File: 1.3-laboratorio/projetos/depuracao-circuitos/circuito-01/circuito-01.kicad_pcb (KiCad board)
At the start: 2 copper layers, 63.5 x 58.4 mm, 19 parts, among them J1 J1, J2 J2, J3 J3, J4 J4, P1 CONN_01X02, SW1 SW_DIP_x04, U1 74LS32, U2 7400, U3 74LS386

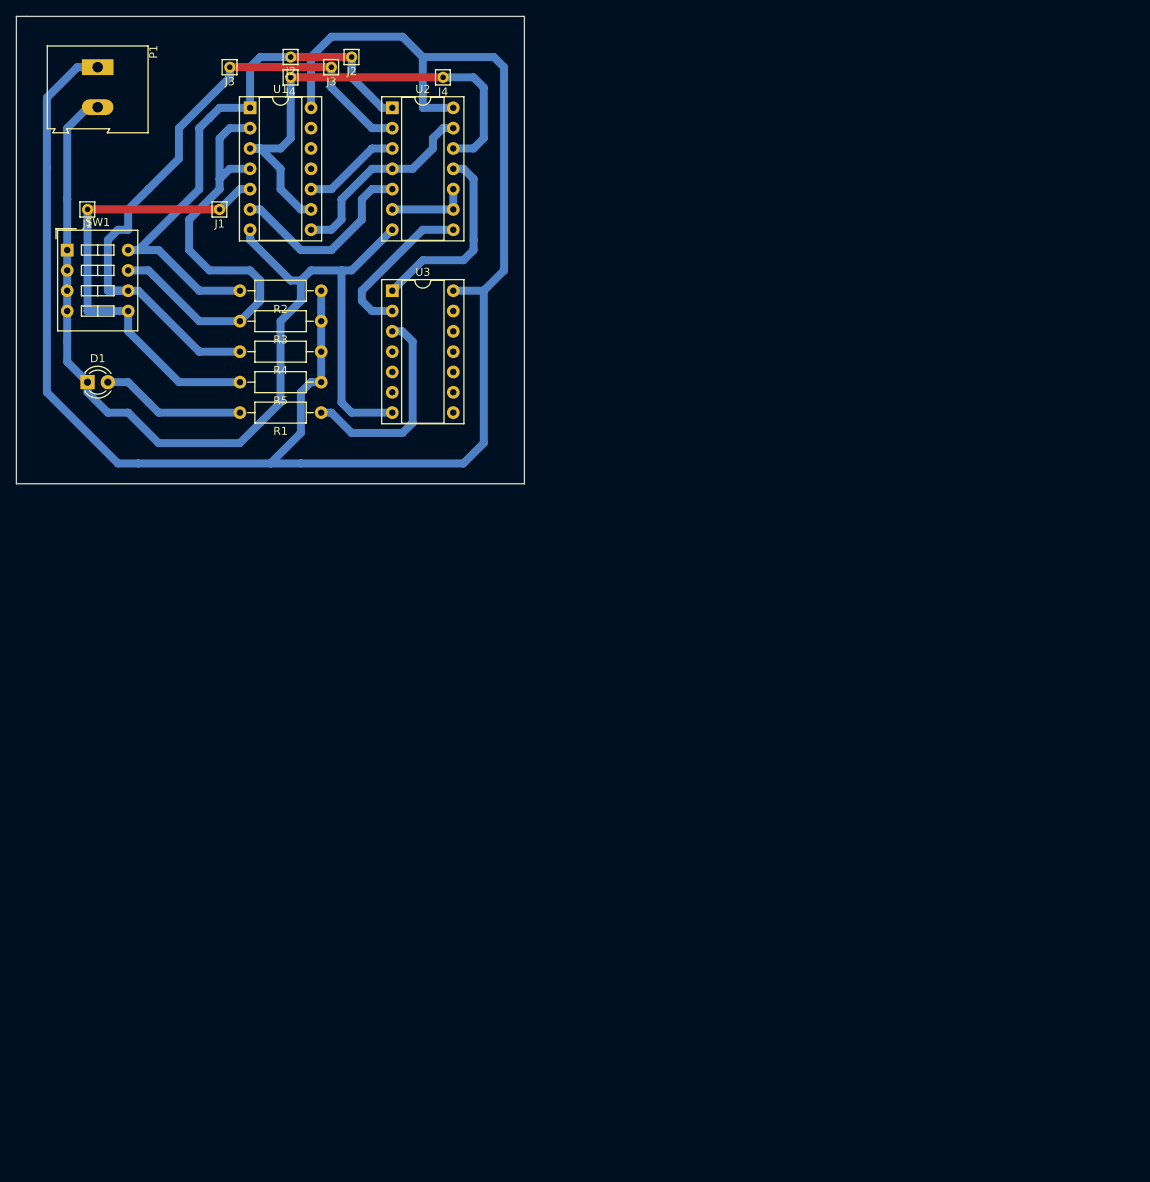
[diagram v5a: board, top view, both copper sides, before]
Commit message: Posicionamento dos componentes na placa. Questão: diminuir a largura e aumentar o comprimento?
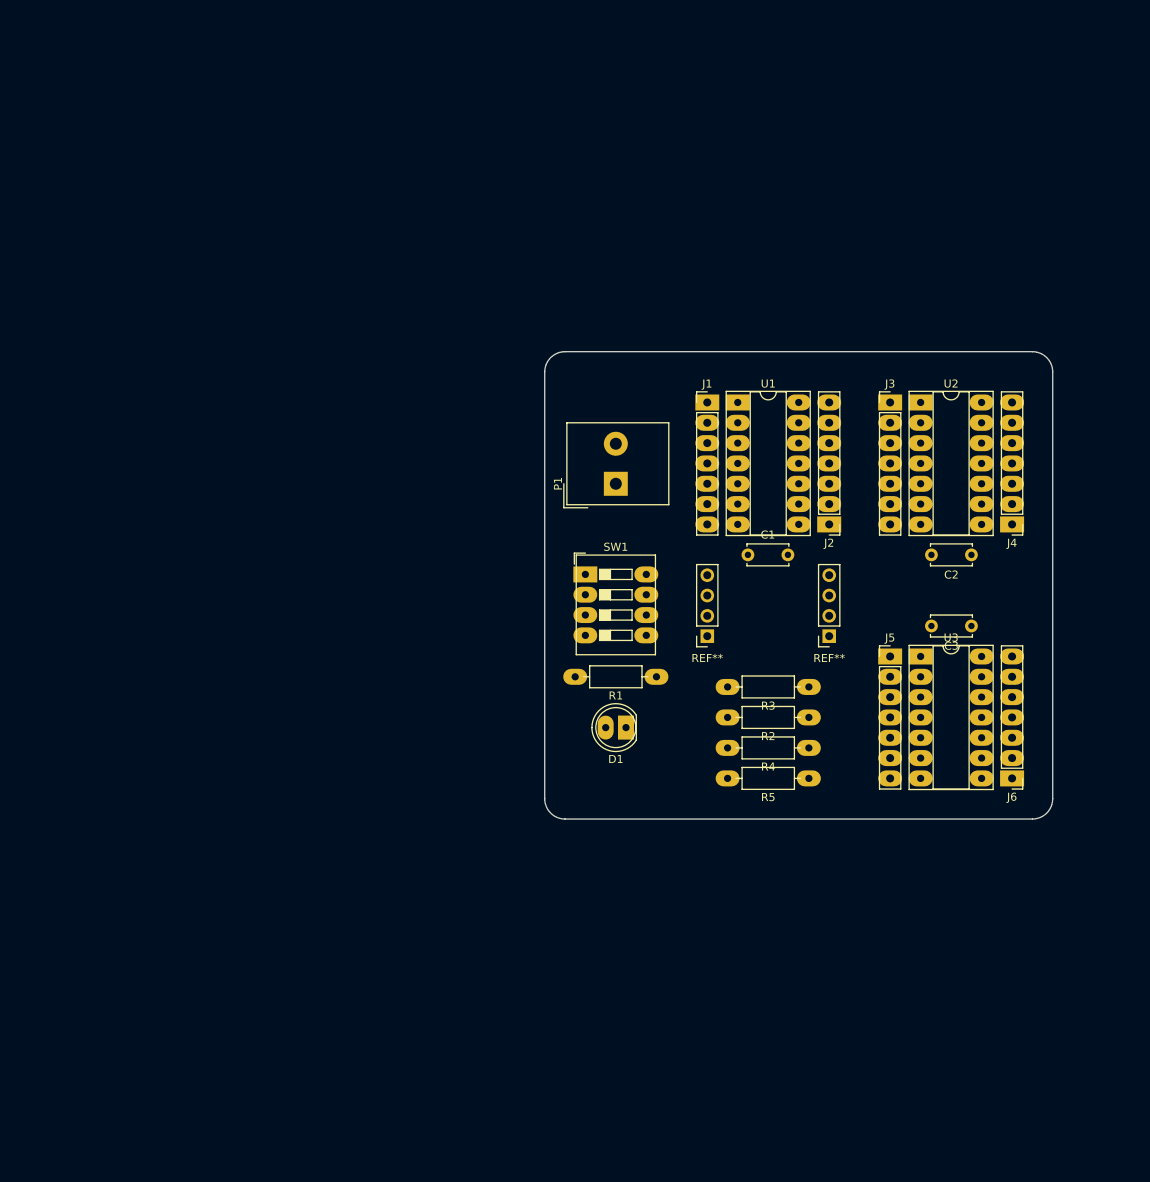
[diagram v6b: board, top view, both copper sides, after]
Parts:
- removed the J1 at (81.3, 61.0)
- removed the J1 at (97.8, 61.0)
- removed the J2 at (106.7, 41.9)
- removed the J2 at (114.3, 41.9)
- removed the J3 at (99.1, 43.2)
- removed the J3 at (111.8, 43.2)
- removed the J4 at (125.7, 44.5)
- removed the J4 at (106.7, 44.5)
- added C1: 10nF, Capacitor_THT:C_Disc_D5.0mm_W2.5mm_P5.00mm, F.Cu at (163.8, 104.1)
- added C2: 10nF, Capacitor_THT:C_Disc_D5.0mm_W2.5mm_P5.00mm, F.Cu at (191.8, 104.1)
- added C3: 10nF, Capacitor_THT:C_Disc_D5.0mm_W2.5mm_P5.00mm, F.Cu at (191.8, 113.0)
- added J1: Conn_01x07_Male, Connector_PinHeader_2.54mm:PinHeader_1x07_P2.54mm_Vertical, F.Cu at (158.8, 85.1)
- added J2: Conn_01x07_Male, Connector_PinHeader_2.54mm:PinHeader_1x07_P2.54mm_Vertical, F.Cu at (174.0, 100.3)
- added J3: Conn_01x07_Male, Connector_PinHeader_2.54mm:PinHeader_1x07_P2.54mm_Vertical, F.Cu at (181.6, 85.1)
- added J4: Conn_01x07_Male, Connector_PinHeader_2.54mm:PinHeader_1x07_P2.54mm_Vertical, F.Cu at (196.8, 100.3)
- added J5: Conn_01x07_Male, Connector_PinHeader_2.54mm:PinHeader_1x07_P2.54mm_Vertical, F.Cu at (181.6, 116.8)
- added J6: Conn_01x07_Male, Connector_PinHeader_2.54mm:PinHeader_1x07_P2.54mm_Vertical, F.Cu at (196.8, 132.1)
- added REF**: PinSocket_1x04_P2.54mm_Vertical, Connector_PinSocket_2.54mm:PinSocket_1x04_P2.54mm_Vertical, F.Cu at (158.8, 114.3)
- added REF**: PinSocket_1x04_P2.54mm_Vertical, Connector_PinSocket_2.54mm:PinSocket_1x04_P2.54mm_Vertical, F.Cu at (174.0, 114.3)
- D1: value LED -> LED_ALT; footprint LEDs:LED_D3.0mm -> LED_THT:LED_D5.0mm
- P1: footprint Terminal_Blocks:TerminalBlock_Altech_AK300-2_P5.00mm -> TerminalBlock_Altech:Altech_AK300_1x02_P5.00mm_45-Degree
- R1: value R -> 270; footprint Resistors_ThroughHole:R_Axial_DIN0207_L6.3mm_D2.5mm_P10.16mm_Horizontal -> Resistor_THT:R_Axial_DIN0207_L6.3mm_D2.5mm_P10.16mm_Horizontal
- R2, R3, R4, R5: value R -> 10k; footprint Resistors_ThroughHole:R_Axial_DIN0207_L6.3mm_D2.5mm_P10.16mm_Horizontal -> Resistor_THT:R_Axial_DIN0207_L6.3mm_D2.5mm_P10.16mm_Horizontal
- SW1: footprint Buttons_Switches_ThroughHole:SW_DIP_x4_W7.62mm_Slide -> Button_Switch_THT:SW_DIP_SPSTx04_Slide_9.78x12.34mm_W7.62mm_P2.54mm
- U1, U2, U3: footprint Housings_DIP:DIP-14_W7.62mm_Socket -> Package_DIP:DIP-14_W7.62mm_Socket_LongPads
- moved P1 83.1 mm to (147.3, 95.2), turned to 90 degrees
- moved R2 81.0 mm to (171.4, 124.5)
- moved U3 80.3 mm to (185.4, 116.8)
- moved D1 80.0 mm to (148.6, 125.7), turned to 180 degrees
- moved R4 78.5 mm to (171.4, 128.3)
- moved R5 78.5 mm to (171.4, 132.1)
- moved SW1 76.4 mm to (143.5, 106.6)
- moved R3 76.2 mm to (171.4, 120.7)
- moved U2 75.6 mm to (185.4, 85.1)
- moved U1 71.2 mm to (162.6, 85.1)
- moved R1 53.4 mm to (152.4, 119.4)
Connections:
- net Net-(R1-Pad1) renamed /U3-03
- net Net-(R2-Pad2) renamed /U1-01
- net Net-(R3-Pad2) renamed /U1-02
- net Net-(R4-Pad2) renamed /U2-02
- net Net-(R5-Pad2) renamed /U1-05
- net Net-(U1-Pad10) renamed /U1-10
- net Net-(U1-Pad3) renamed /U1-03
- net Net-(U1-Pad6) renamed /U1-06
- net Net-(U1-Pad8) renamed /U1-08
- net Net-(U2-Pad10) renamed /U2-06
- net Net-(U2-Pad11) renamed /U2-11
- net Net-(U2-Pad8) renamed /U2-08
- U1 pad 11: (no net) -> /U1-11
- U1 pad 12: (no net) -> /U1-12
- U1 pad 13: (no net) -> /U1-13
- U3 pad 10: (no net) -> /U3-10
- U3 pad 11: (no net) -> /U3-11
- U3 pad 12: (no net) -> /U3-12
- U3 pad 13: (no net) -> /U3-13
- U3 pad 4: (no net) -> /U3-04
- U3 pad 5: (no net) -> /U3-05
- U3 pad 6: (no net) -> /U3-06
- U3 pad 8: (no net) -> /U3-08
- U3 pad 9: (no net) -> /U3-09
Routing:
- net VCC: track 224.2 -> 0.00 mm
- net GND: track 131.4 -> 0.00 mm
- net /U2-02: track 69.5 -> 0.00 mm
- net /U1-01: track 65.6 -> 0.00 mm
- net /U1-02: track 57.4 -> 0.00 mm
- net (no net): track 55.9 -> 0.00 mm
- net /U1-03: track 41.8 -> 0.00 mm
- net /U1-05: track 41.8 -> 0.00 mm
- net /U3-03: track 26.2 -> 0.00 mm
- net /U1-08: track 25.3 -> 0.00 mm
- net /U1-06: track 24.5 -> 0.00 mm
- net /U2-11: track 24.2 -> 0.00 mm
- net /U2-08: track 20.2 -> 0.00 mm
- net Net-(D1-Pad2): track 18.1 -> 0.00 mm
- net /U1-10: track 12.3 -> 0.00 mm
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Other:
- outline, holes or cut-outs redrawn
- net class Alimentacao: clearance 0.5 -> 0.508; trace_width 1 -> 0.5; via_dia 0.6 -> 2; via_drill 0.4 -> 0.9
- net class Default: clearance 0.5 -> 0.508; trace_width 1 -> 0.5; via_dia 0.6 -> 2; via_drill 0.4 -> 0.9
- rule trace_clearance: 0.5 -> 0.508
- rule trace_min: 0.2 -> 0.5
- rule via_min_drill: 0.3 -> 0.4
- rule via_min_size: 0.4 -> 0.6

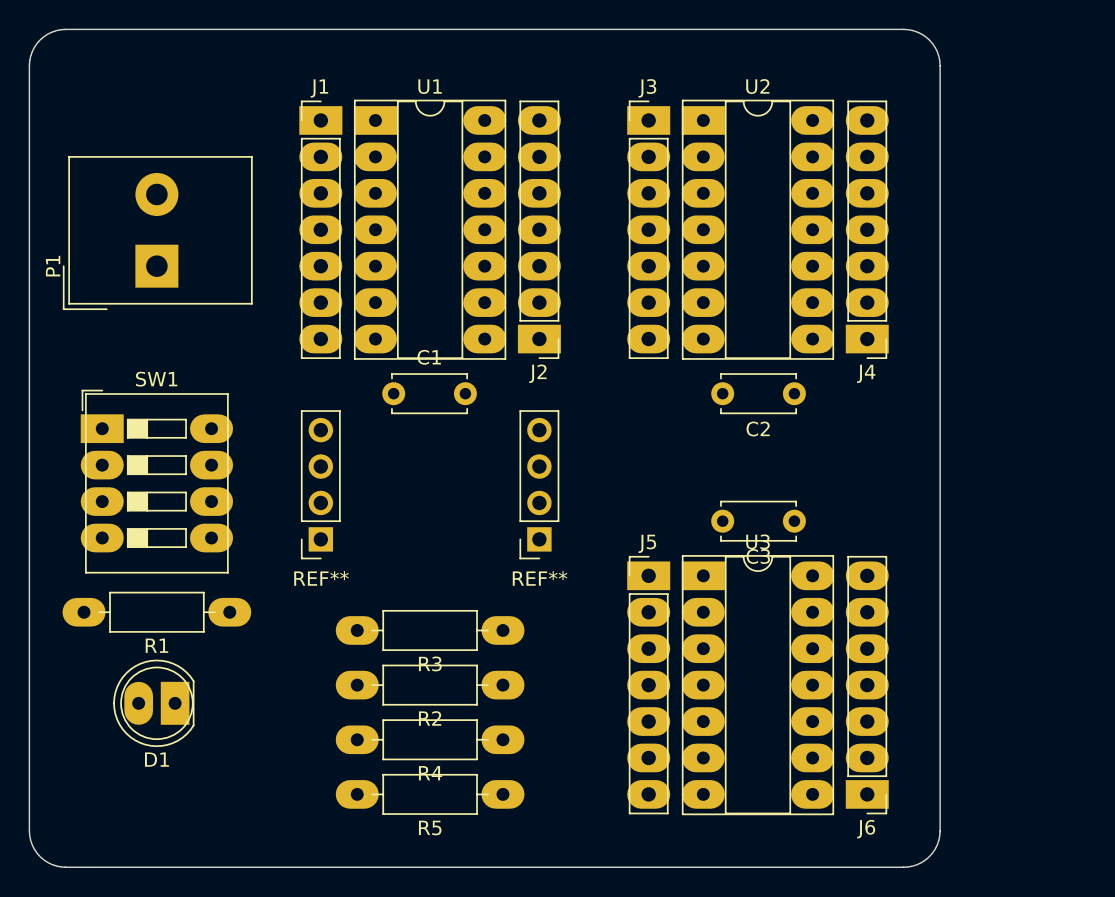
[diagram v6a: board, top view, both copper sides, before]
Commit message: Leiaute promissor para Circuito 01.
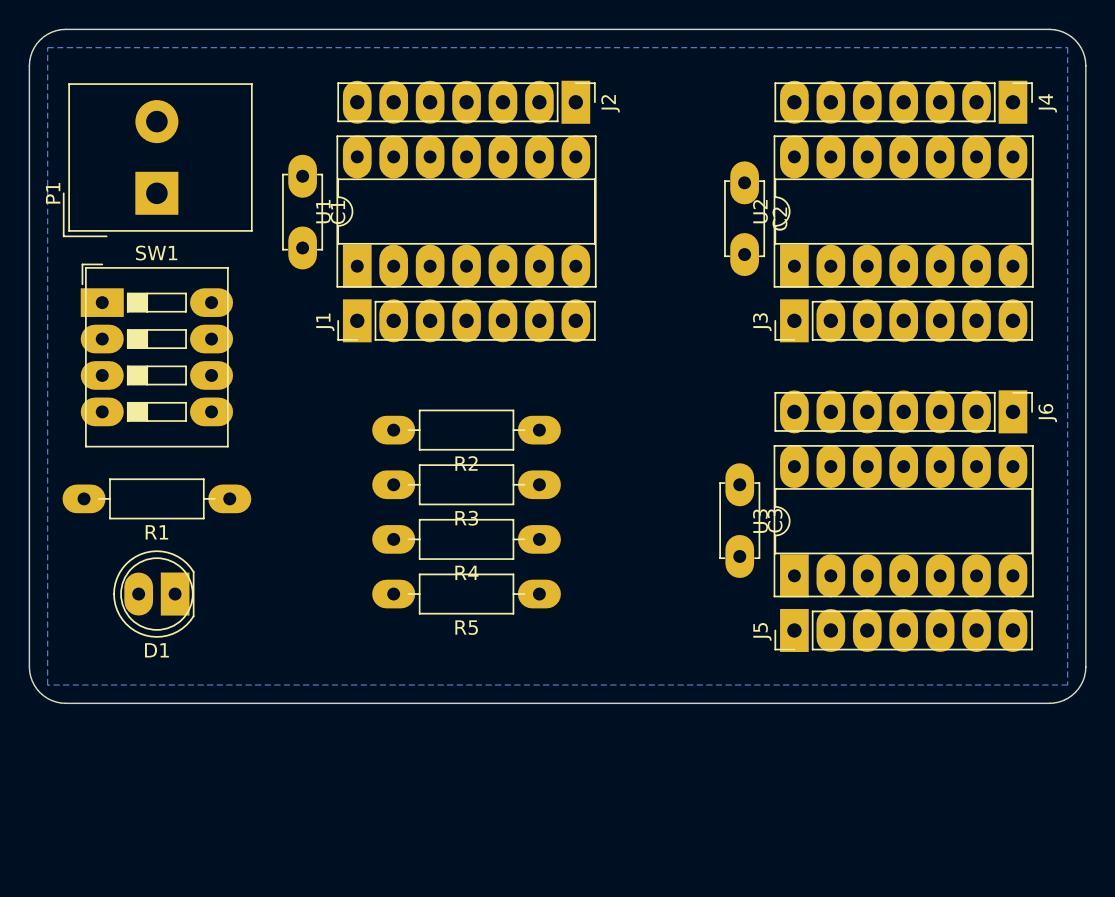
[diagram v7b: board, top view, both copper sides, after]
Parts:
- removed REF** (x2): PinSocket_1x04_P2.54mm_Vertical, Connector_PinSocket_2.54mm:PinSocket_1x04_P2.54mm_Vertical
- moved J6 28.5 mm to (207.0, 105.4), turned to 270 degrees
- moved J4 19.4 mm to (207.0, 83.8), turned to 270 degrees
- moved R2 18.0 mm to (174.0, 106.7)
- moved J3 17.3 mm to (191.8, 99.1), turned to 90 degrees
- moved J2 16.7 mm to (176.5, 83.8), turned to 270 degrees
- moved C1 16.4 mm to (157.5, 89.0), turned to 270 degrees
- moved C2 15.1 mm to (188.3, 89.4), turned to 270 degrees
- moved R4 14.2 mm to (174.0, 114.3)
- moved R5 14.2 mm to (174.0, 118.1)
- moved J1 14.2 mm to (161.3, 99.1), turned to 90 degrees
- moved U2 12.0 mm to (191.8, 95.2), turned to 90 degrees
- moved J5 10.9 mm to (191.8, 120.7), turned to 90 degrees
- moved R3 10.5 mm to (174.0, 110.5)
- moved U1 10.2 mm to (161.3, 95.2), turned to 90 degrees
- moved SW1 8.79 mm to (143.5, 97.8)
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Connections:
- J5 pad 1: /U2-11 -> /U3-01
- J5 pad 2: /U2-08 -> /U3-02
- J6 pad 1: /U3-08 -> /U2-11
- J6 pad 2: /U3-09 -> /U2-08
- P1 pad 1: VCC -> GND
- P1 pad 2: GND -> VCC
- R1 pad 1: /U3-03 -> /U3-10
- U3 pad 1: /U2-11 -> /U3-01
- U3 pad 2: /U2-08 -> /U3-02
- U3 pad 8: /U3-08 -> /U2-11
- U3 pad 9: /U3-09 -> /U2-08
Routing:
- added copper zone on B.Cu, net GND
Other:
- board size 63.5 x 58.4 mm -> 73.7 x 47 mm

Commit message: Leiaute em elaboração para o Circuito 01.
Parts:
- added J7: Conn_01x04, Connector_PinSocket_2.54mm:PinSocket_1x04_P2.54mm_Vertical, F.Cu at (179.1, 102.9)
- added J8: Conn_01x04, Connector_PinSocket_2.54mm:PinSocket_1x04_P2.54mm_Vertical, F.Cu at (163.8, 102.9)
- moved R3 8.03 mm to (176.5, 118.1)
- moved R4 8.03 mm to (176.5, 121.9)
- moved R5 8.03 mm to (176.5, 125.7)
- moved R2 8.03 mm to (176.5, 114.3)
- moved C3 5.08 mm to (188.0, 115.6)
- moved J5 5.08 mm to (191.8, 125.7)
- moved J6 5.08 mm to (207.0, 110.5)
- moved U3 5.08 mm to (191.8, 121.9)
- moved C1 2.54 mm to (160.0, 89.0)
- moved J1 2.54 mm to (163.8, 99.1)
- moved U1 2.54 mm to (163.8, 95.2)
- moved J2 2.54 mm to (179.1, 83.8)
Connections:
- R3 pad 2: /U1-02 -> /U2-02
- R4 pad 2: /U2-02 -> /U1-02
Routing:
- net VCC: track 0.00 -> 175.5 mm
- net /U1-03: track 0.00 -> 86.6 mm, vias 0 -> 2
- net /U1-01: track 0.00 -> 70.9 mm
- net /U2-02: track 0.00 -> 67.0 mm
- net /U1-05: track 0.00 -> 63.0 mm
- net /U3-10: track 0.00 -> 55.9 mm
- net /U1-06: track 0.00 -> 50.2 mm
- net /U1-08: track 0.00 -> 38.6 mm
- net /U1-02: track 0.00 -> 37.4 mm
- net /U2-06: track 0.00 -> 21.6 mm
- net Net-(D1-Pad2): track 0.00 -> 8.51 mm
- net /U2-11: track 0.00 -> 7.62 mm
- net /U2-08: track 0.00 -> 7.62 mm
- net /U1-10: track 0.00 -> 7.62 mm
- net /U3-13: track 0.00 -> 3.81 mm
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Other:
- board size 73.7 x 47 mm -> 73.7 x 52.1 mm
